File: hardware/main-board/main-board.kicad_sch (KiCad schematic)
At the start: 85 parts, among them J1 USB_C_Receptacle_USB2.0, J2 DNI, J3 Display Connector, J4 Conn_01x02, SW1 SW_Push, SW2 SW_Push, SW3 SW_Push, SW4 SW_Push, SW5 SW_Detect, SW6 SW_Boot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

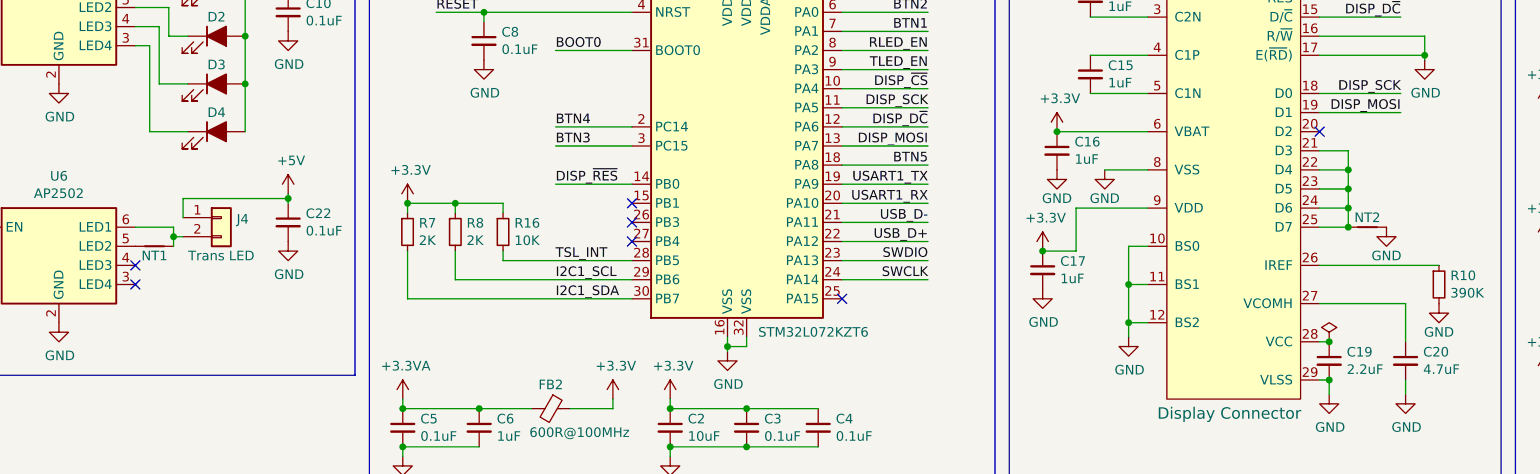
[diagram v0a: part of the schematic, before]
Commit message: Update symbol pins and remove net ties
Fix #27
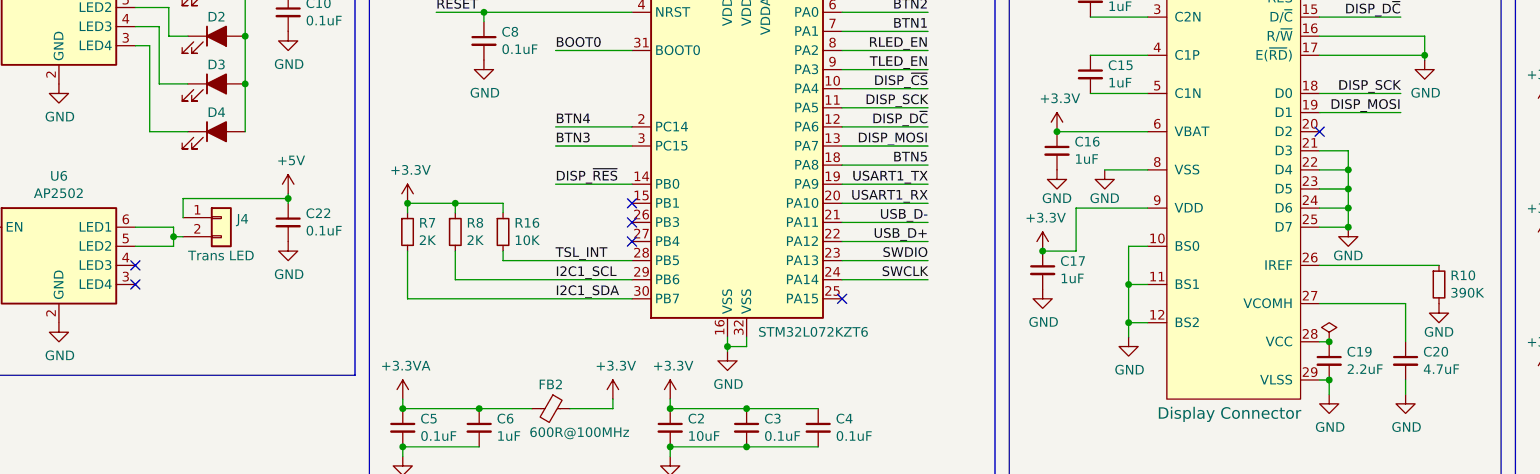
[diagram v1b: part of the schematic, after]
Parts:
- removed NT1: Net-Tie_2, lib_fp:NetTie-2_SMD_Pad_20mil, symbol Device:NetTie_2
- removed NT2: Net-Tie_2, lib_fp:NetTie-2_SMD_Pad_10mil, symbol Device:NetTie_2
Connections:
- net GND: now also J3.21 (D3), J3.22 (D4), J3.23 (D5), J3.24 (D6), J3.25 (D7)
- net at U6.5 (LED2): now also J4.2 (Pin_2), U6.6 (LED1)
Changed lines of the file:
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@@
   (junction (at 299.085 27.94) (diameter 0) (color 0 0 0 0)
   )
+  (junction (at 250.19 58.42) (diameter 0) (color 0 0 0 0)
+  )
   (junction (at 28.575 147.955) (diameter 0) (color 0 0 0 0)
   )
@@
   (junction (at 130.175 109.855) (diameter 0) (color 0 0 0 0)
   )
-  (junction (at 250.19 58.42) (diameter 0) (color 0 0 0 0)
-  )
   (junction (at 103.505 33.02) (diameter 0) (color 0 0 0 0)
   )
@@
     (stroke (width 0) (type default) (color 0 0 0 0))
   )
+  (wire (pts (xy 88.9 60.96) (xy 93.98 60.96))
+    (stroke (width 0) (type default) (color 0 0 0 0))
+  )
   (wire (pts (xy 257.81 68.58) (xy 257.81 73.66))
     (stroke (width 0) (type default) (color 0 0 0 0))
@@
     (pin "6")
   )
-  (symbol (lib_id "Device:NetTie_2") (at 91.44 60.96 0) (unit 1)
-    (in_bom no) (on_board yes)
-    (property "Reference" "NT1" (id 0) (at 91.44 62.23 0))
-    (property "Value" "Net-Tie_2" (id 1) (at 91.44 58.674 0)
-      (effects (font (size 1.27 1.27)) hide)
-    )
-    (property "Footprint" "lib_fp:NetTie-2_SMD_Pad_20mil" (id 2) (at 91.44 60.96 0)
-      (effects (font (size 1.27 1.27)) hide)
-    )
-    (property "Datasheet" "~" (id 3) (at 91.44 60.96 0)
-      (effects (font (size 1.27 1.27)) hide)
-    )
-    (pin "1")
-    (pin "2")
-  )
   (symbol (lib_id "Project:AP2502") (at 78.74 62.23 0) (unit 1)
     (in_bom yes) (on_board yes)
@@
     (pin "2")
   )
-  (symbol (lib_id "Device:NetTie_2") (at 252.73 58.42 0) (unit 1)
-    (in_bom no) (on_board yes)
-    (property "Reference" "NT2" (id 0) (at 252.73 57.15 0))
-    (property "Value" "Net-Tie_2" (id 1) (at 252.73 56.134 0)
-      (effects (font (size 1.27 1.27)) hide)
-    )
-    (property "Footprint" "lib_fp:NetTie-2_SMD_Pad_10mil" (id 2) (at 252.73 58.42 0)
-      (effects (font (size 1.27 1.27)) hide)
-    )
-    (property "Datasheet" "~" (id 3) (at 252.73 58.42 0)
-      (effects (font (size 1.27 1.27)) hide)
-    )
-    (pin "1")
-    (pin "2")
-  )
   (symbol (lib_id "Device:Polyfuse") (at 107.95 109.855 270) (unit 1)
     (in_bom yes) (on_board yes)
@@
     )
   )
-  (symbol (lib_id "power:GND") (at 255.27 58.42 0) (unit 1)
+  (symbol (lib_id "power:GND") (at 250.19 58.42 0) (unit 1)
     (in_bom yes) (on_board yes)
-    (property "Reference" "#PWR05" (id 0) (at 255.27 64.77 0)
+    (property "Reference" "#PWR05" (id 0) (at 250.19 64.77 0)
       (effects (font (size 1.27 1.27)) hide)
     )
-    (property "Value" "GND" (id 1) (at 255.27 62.23 0))
-    (property "Footprint" "" (id 2) (at 255.27 58.42 0)
+    (property "Value" "GND" (id 1) (at 250.19 62.23 0))
+    (property "Footprint" "" (id 2) (at 250.19 58.42 0)
       (effects (font (size 1.27 1.27)) hide)
     )
-    (property "Datasheet" "" (id 3) (at 255.27 58.42 0)
+    (property "Datasheet" "" (id 3) (at 250.19 58.42 0)
       (effects (font (size 1.27 1.27)) hide)
     )
@@
       (reference "J4") (unit 1) (value "Conn_01x02") (footprint "Connector_JST:JST_SH_BM02B-SRSS-TB_1x02-1MP_P1.00mm_Vertical")
     )
-    (path "/00000000-0000-0000-0000-000060ba0beb"
-      (reference "NT1") (unit 1) (value "Net-Tie_2") (footprint "lib_fp:NetTie-2_SMD_Pad_20mil")
-    )
-    (path "/00000000-0000-0000-0000-000060c06ad9"
-      (reference "NT2") (unit 1) (value "Net-Tie_2") (footprint "lib_fp:NetTie-2_SMD_Pad_10mil")
-    )
     (path "/00000000-0000-0000-0000-00006056cdf1"

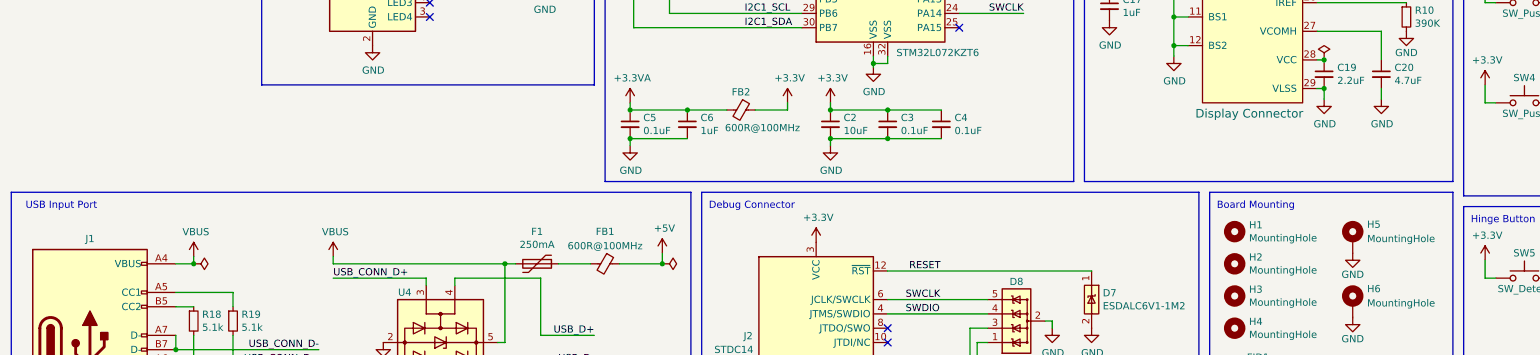
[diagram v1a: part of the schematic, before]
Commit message: Add display note to the schematic
Fix #28
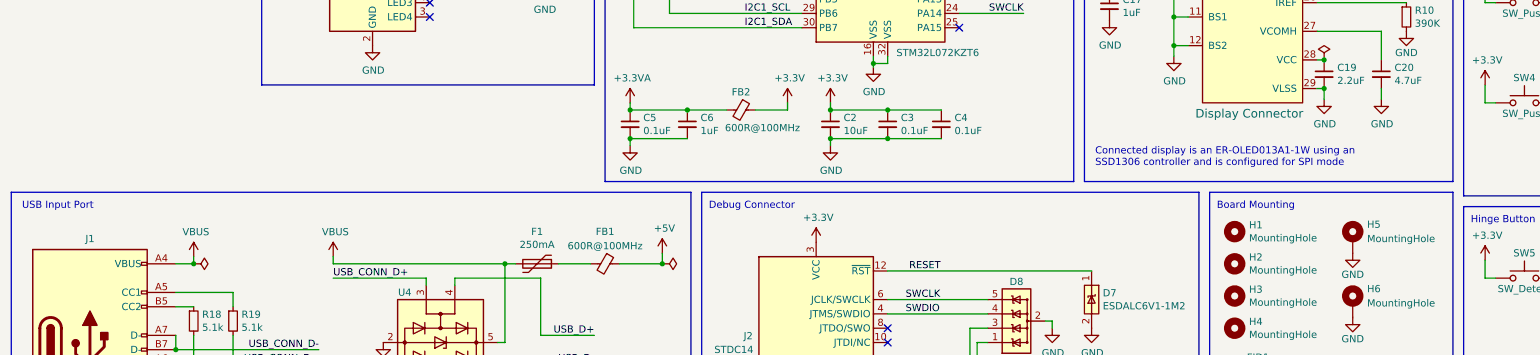
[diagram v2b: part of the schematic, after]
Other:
- note added: "Connected display is an ER-OLED013A1-1W using an SSD1306 controller and is configured for SPI mode"
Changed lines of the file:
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@@
     (effects (font (size 1.27 1.27)) (justify left bottom))
   )
-  (text "USB Input Port" (at 17.145 100.33 0)
+  (text "USB Input Port" (at 16.51 100.33 0)
     (effects (font (size 1.27 1.27)) (justify left bottom))
   )
@@
     (effects (font (size 1.27 1.27)) (justify left bottom))
   )
+  (text "Connected display is an ER-OLED013A1-1W using an\nSSD1306 controller and is configured for SPI mode"
+    (at 207.01 92.71 0)
+    (effects (font (size 1.27 1.27)) (justify left bottom))
+  )

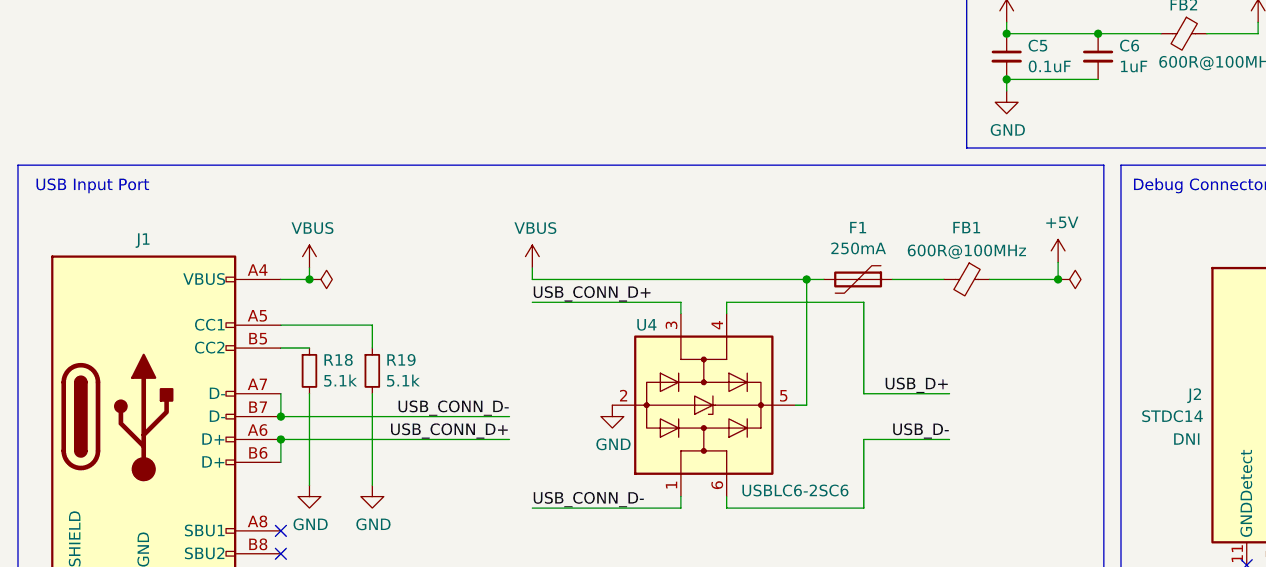
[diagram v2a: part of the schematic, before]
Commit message: Add bulk capacitor to VBUS input
Added a 4.7uF capacitor just past the VBUS input ferrite bead, before
the +5V line goes to the 5V power plane.
Decided to stick with 4.7uF instead of 10uF for component commonality
and to avoid going past 10uF when including the LDO input capacitor.

Changed the 4.7uF capacitor used in both areas of the design to one with
a 25V rating, just to be safe.

Updated PCB layout and nudged some silkscreen bits around.

Fix #26
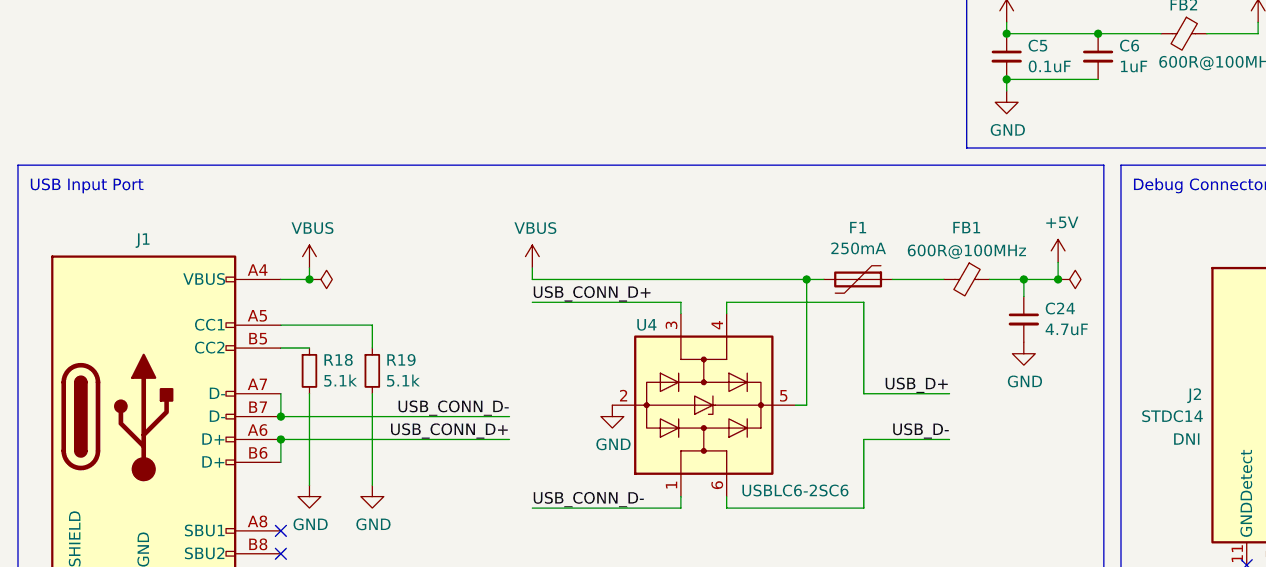
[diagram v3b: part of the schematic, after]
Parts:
- added C24: 4.7uF, Capacitor_SMD:C_0603_1608Metric, symbol Device:C_Small
- C20: Manufacturer TDK Corporation -> Samsung Electro-Mechanics; Manufacturer PN C1608X5R1C475K080AC -> CL10A475KA8NQNC; Supplier PN 445-7478-1-ND -> 1276-1900-1-ND
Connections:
- net +5V: now also C24.1
- net GND: now also C24.2
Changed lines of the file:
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@@
   (junction (at 46.99 109.855) (diameter 0) (color 0 0 0 0)
   )
+  (junction (at 126.365 109.855) (diameter 0) (color 0 0 0 0)
+  )
   (junction (at 102.235 109.855) (diameter 0) (color 0 0 0 0)
   )
@@
     (stroke (width 0) (type default) (color 0 0 0 0))
   )
-  (wire (pts (xy 122.555 109.855) (xy 130.175 109.855))
+  (wire (pts (xy 122.555 109.855) (xy 126.365 109.855))
     (stroke (width 0) (type default) (color 0 0 0 0))
   )
@@
     (stroke (width 0) (type default) (color 0 0 0 0))
   )
+  (wire (pts (xy 126.365 109.855) (xy 130.175 109.855))
+    (stroke (width 0) (type default) (color 0 0 0 0))
+  )
   (wire (pts (xy 246.38 50.8) (xy 250.19 50.8))
     (stroke (width 0) (type default) (color 0 0 0 0))
@@
     (stroke (width 0) (type default) (color 0 0 0 0))
   )
+  (wire (pts (xy 126.365 109.855) (xy 126.365 111.76))
+    (stroke (width 0) (type default) (color 0 0 0 0))
+  )
   (wire (pts (xy 223.52 40.64) (xy 215.9 40.64))
     (stroke (width 0) (type default) (color 0 0 0 0))
@@
     (effects (font (size 1.27 1.27)) (justify left bottom))
   )
-  (text "USB Input Port" (at 16.51 100.33 0)
+  (text "USB Input Port" (at 15.875 100.33 0)
     (effects (font (size 1.27 1.27)) (justify left bottom))
   )
@@
       (effects (font (size 1.27 1.27)) hide)
     )
-    (property "Datasheet" "~" (id 3) (at 99.695 26.67 0)
+    (property "Datasheet" "https://katalog.we-online.de/led/datasheet/158302250.pdf" (id 3) (at 99.695 26.67 0)
       (effects (font (size 1.27 1.27)) hide)
     )
@@
       (effects (font (size 1.27 1.27)) hide)
     )
-    (property "Datasheet" "~" (id 3) (at 120.015 109.855 0)
+    (property "Datasheet" "https://media.digikey.com/pdf/Data%20Sheets/TDK%20PDFs/MMZ_Series_Br.pdf" (id 3) (at 120.015 109.855 0)
       (effects (font (size 1.27 1.27)) hide)
     )
@@
       (effects (font (size 1.27 1.27)) hide)
     )
-    (property "Datasheet" "~" (id 3) (at 144.145 82.55 0)
+    (property "Datasheet" "https://media.digikey.com/pdf/Data%20Sheets/TDK%20PDFs/MMZ_Series_Br.pdf" (id 3) (at 144.145 82.55 0)
       (effects (font (size 1.27 1.27)) hide)
     )
@@
       (effects (font (size 1.27 1.27)) hide)
     )
-    (property "Datasheet" "https://product.tdk.com/info/en/catalog/datasheets/mlcc_commercial_general_en.pdf" (id 3) (at 257.81 76.2 0)
+    (property "Datasheet" "http://www.samsungsem.com/kr/support/product-search/mlcc/CL10A475KA8NQNC.jsp" (id 3) (at 257.81 76.2 0)
       (effects (font (size 1.27 1.27)) hide)
     )
-    (property "Description" "CAP CER 4.7UF 16V X5R 0603" (id 4) (at 257.81 76.2 0)
+    (property "Description" "CAP CER 4.7UF 25V X5R 0603" (id 4) (at 257.81 76.2 0)
       (effects (font (size 1.27 1.27)) hide)
     )
-    (property "Manufacturer" "TDK Corporation" (id 5) (at 257.81 76.2 0)
+    (property "Manufacturer" "Samsung Electro-Mechanics" (id 5) (at 257.81 76.2 0)
       (effects (font (size 1.27 1.27)) hide)
     )
-    (property "Manufacturer PN" "C1608X5R1C475K080AC" (id 6) (at 257.81 76.2 0)
+    (property "Manufacturer PN" "CL10A475KA8NQNC" (id 6) (at 257.81 76.2 0)
       (effects (font (size 1.27 1.27)) hide)
     )
@@
       (effects (font (size 1.27 1.27)) hide)
     )
-    (property "Supplier PN" "445-7478-1-ND" (id 8) (at 257.81 76.2 0)
+    (property "Supplier PN" "1276-1900-1-ND" (id 8) (at 257.81 76.2 0)
       (effects (font (size 1.27 1.27)) hide)
     )
@@
     (pin "1")
   )
+  (symbol (lib_id "Device:C_Small") (at 126.365 114.3 0) (unit 1)
+    (in_bom yes) (on_board yes)
+    (property "Reference" "C24" (id 0) (at 128.7018 113.1316 0)
+      (effects (font (size 1.27 1.27)) (justify left))
+    )
+    (property "Value" "4.7uF" (id 1) (at 128.7018 115.443 0)
+      (effects (font (size 1.27 1.27)) (justify left))
+    )
+    (property "Footprint" "Capacitor_SMD:C_0603_1608Metric" (id 2) (at 126.365 114.3 0)
+      (effects (font (size 1.27 1.27)) hide)
+    )
+    (property "Datasheet" "http://www.samsungsem.com/kr/support/product-search/mlcc/CL10A475KA8NQNC.jsp" (id 3) (at 126.365 114.3 0)
+      (effects (font (size 1.27 1.27)) hide)
+    )
+    (property "Description" "CAP CER 4.7UF 25V X5R 0603" (id 4) (at 126.365 114.3 0)
+      (effects (font (size 1.27 1.27)) hide)
+    )
+    (property "Manufacturer" "Samsung Electro-Mechanics" (id 5) (at 126.365 114.3 0)
+      (effects (font (size 1.27 1.27)) hide)
+    )
+    (property "Manufacturer PN" "CL10A475KA8NQNC" (id 6) (at 126.365 114.3 0)
+      (effects (font (size 1.27 1.27)) hide)
+    )
+    (property "Supplier" "Digi-Key" (id 7) (at 126.365 114.3 0)
+      (effects (font (size 1.27 1.27)) hide)
+    )
+    (property "Supplier PN" "1276-1900-1-ND" (id 8) (at 126.365 114.3 0)
+      (effects (font (size 1.27 1.27)) hide)
+    )
+    (pin "1")
+    (pin "2")
+  )
+  (symbol (lib_id "power:GND") (at 126.365 116.84 0) (unit 1)
+    (in_bom yes) (on_board yes)
+    (property "Reference" "#PWR023" (id 0) (at 126.365 123.19 0)
+      (effects (font (size 1.27 1.27)) hide)
+    )
+    (property "Value" "GND" (id 1) (at 126.492 121.2342 0))
+    (property "Footprint" "" (id 2) (at 126.365 116.84 0)
+      (effects (font (size 1.27 1.27)) hide)
+    )
+    (property "Datasheet" "" (id 3) (at 126.365 116.84 0)
+      (effects (font (size 1.27 1.27)) hide)
+    )
+    (pin "1")
+  )
   (sheet_instances
     (path "/" (page "1"))
@@
       (reference "#PWR022") (unit 1) (value "GND") (footprint "")
     )
+    (path "/fd8c1a00-cde3-4aa6-bfba-737d79ee002f"
+      (reference "#PWR023") (unit 1) (value "GND") (footprint "")
+    )
     (path "/00000000-0000-0000-0000-00006056b42f"
       (reference "#PWR0101") (unit 1) (value "GND") (footprint "")
@@
       (reference "C23") (unit 1) (value "0.1uF") (footprint "Capacitor_SMD:C_0603_1608Metric")
     )
+    (path "/004d701c-7e69-4a10-9c95-7de04fa2be20"
+      (reference "C24") (unit 1) (value "4.7uF") (footprint "Capacitor_SMD:C_0603_1608Metric")
+    )
     (path "/00000000-0000-0000-0000-00006056c6a5"
